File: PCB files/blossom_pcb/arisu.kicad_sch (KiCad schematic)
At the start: 40 parts, among them P1 Conn_ARM_JTAG_SWD_10

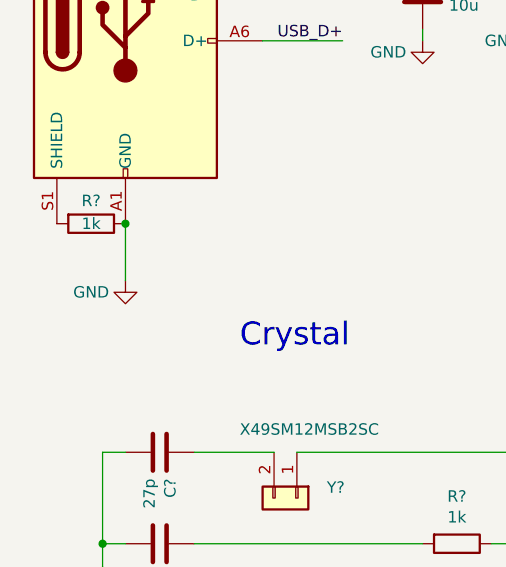
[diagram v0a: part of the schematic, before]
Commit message: Fixed part numbers for JLCPCB
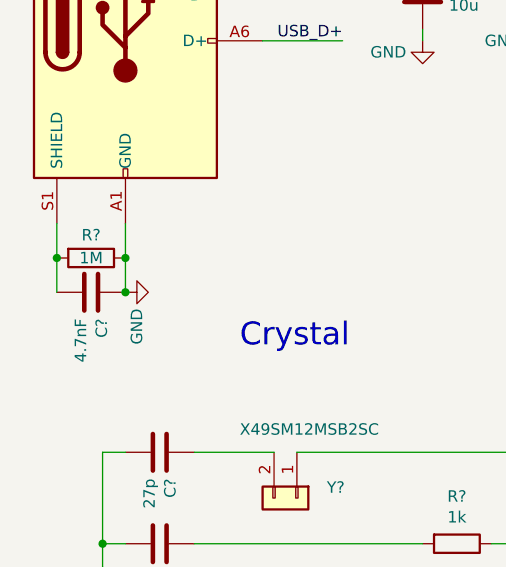
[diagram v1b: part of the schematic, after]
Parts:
- removed R?: 1k, Resistor_SMD:R_01005_0402Metric, symbol arisu-rescue:R-Device
- added C?: 4.7nF, Capacitor_SMD:C_0201_0603Metric, symbol arisu-rescue:C-Device
- added R?: 1M, Resistor_SMD:R_0805_2012Metric, symbol arisu-rescue:R-Device
- R? (x2): MPN (none) -> C104384
- USB1: MPN (none) -> C134092
- Y?: MPN (none) -> C110563
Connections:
- net GND: now also C?.1, R?.1
- net at USB1.S1 (SHIELD): now also C?.2, R?.2
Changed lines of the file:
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@@
   (junction (at 158.75 43.18) (diameter 0) (color 0 0 0 0)
   )
-  (junction (at 26.67 59.69) (diameter 0) (color 0 0 0 0)
-  )
   (junction (at 158.75 48.26) (diameter 0) (color 0 0 0 0)
   )
@@
   (junction (at 121.92 43.18) (diameter 0) (color 0 0 0 0)
   )
+  (junction (at 26.67 67.31) (diameter 0) (color 0 0 0 0)
+  )
   (junction (at 148.59 48.26) (diameter 0) (color 0 0 0 0)
   )
@@
   (junction (at 172.72 39.37) (diameter 0) (color 0 0 0 0)
   )
+  (junction (at 19.05 63.5) (diameter 0) (color 0 0 0 0)
+  )
   (junction (at 207.01 39.37) (diameter 0) (color 0 0 0 0)
   )
+  (junction (at 26.67 63.5) (diameter 0) (color 0 0 0 0)
+  )
   (junction (at 151.13 48.26) (diameter 0) (color 0 0 0 0)
   )
@@
     (stroke (width 0) (type default))
   )
-  (wire (pts (xy 26.67 66.04) (xy 26.67 59.69))
-    (stroke (width 0) (type default))
-  )
   (bus (pts (xy 220.98 97.79) (xy 220.98 100.33))
     (stroke (width 0) (type default))
@@
     (stroke (width 0) (type default))
   )
+  (wire (pts (xy 19.05 63.5) (xy 19.05 59.69))
+    (stroke (width 0) (type default))
+  )
   (bus (pts (xy 213.36 111.76) (xy 213.36 114.3))
     (stroke (width 0) (type default))
@@
     (stroke (width 0) (type default))
   )
+  (wire (pts (xy 26.67 63.5) (xy 26.67 67.31))
+    (stroke (width 0) (type default))
+  )
   (wire (pts (xy 138.43 27.94) (xy 149.86 27.94))
     (stroke (width 0) (type default))
@@
     (stroke (width 0) (type default))
   )
+  (wire (pts (xy 19.05 63.5) (xy 19.05 67.31))
+    (stroke (width 0) (type default))
+  )
+  (wire (pts (xy 26.67 63.5) (xy 26.67 59.69))
+    (stroke (width 0) (type default))
+  )
   (wire (pts (xy 173.99 114.3) (xy 210.82 114.3))
     (stroke (width 0) (type default))
@@
       (effects (font (size 1.27 1.27)) hide)
     )
+    (property "MPN" "C110563" (at 45.72 90.17 0)
+      (effects (font (size 1.27 1.27)) hide)
+    )
     (pin "1")
     (pin "2")
@@
     )
   )
+  (symbol (lib_id "arisu-rescue:R-Device") (at 22.86 63.5 270) (unit 1)
+    (in_bom yes) (on_board yes) (dnp no)
+    (property "Reference" "R?" (at 22.86 60.96 90)
+      (effects (font (size 1.27 1.27)))
+    )
+    (property "Value" "1M" (at 22.86 63.5 90)
+      (effects (font (size 1.27 1.27)))
+    )
+    (property "Footprint" "Resistor_SMD:R_0805_2012Metric" (at 22.86 61.722 90)
+      (effects (font (size 1.27 1.27)) hide)
+    )
+    (property "Datasheet" "~" (at 22.86 63.5 0)
+      (effects (font (size 1.27 1.27)) hide)
+    )
+    (property "MPN" "C17514" (at 22.86 63.5 0)
+      (effects (font (size 1.27 1.27)) hide)
+    )
+    (pin "1")
+    (pin "2")
+    (instances
+      (project "RP2040_minimal"
+        (path "/4e80874f-13b9-4886-a592-f501191b7905"
+          (reference "R?") (unit 1)
+        )
+      )
+      (project "arisu"
+        (path "/6a4507f9-fb93-401b-b9e1-9f2bcbbd5186"
+          (reference "R9") (unit 1)
+        )
+      )
+    )
+  )
   (symbol (lib_id "PCM_RP2040_minimal-rescue:VBUS-power") (at 29.21 114.3 0) (unit 1)
     (in_bom yes) (on_board yes) (dnp no)
@@
     )
   )
+  (symbol (lib_id "arisu-rescue:C-Device") (at 22.86 67.31 270) (unit 1)
+    (in_bom yes) (on_board yes) (dnp no)
+    (property "Reference" "C?" (at 24.0284 70.231 0)
+      (effects (font (size 1.27 1.27)) (justify left))
+    )
+    (property "Value" "4.7nF" (at 21.717 70.231 0)
+      (effects (font (size 1.27 1.27)) (justify left))
+    )
+    (property "Footprint" "Capacitor_SMD:C_0201_0603Metric" (at 19.05 68.2752 0)
+      (effects (font (size 1.27 1.27)) hide)
+    )
+    (property "Datasheet" "~" (at 22.86 67.31 0)
+      (effects (font (size 1.27 1.27)) hide)
+    )
+    (pin "1")
+    (pin "2")
+    (instances
+      (project "RP2040_minimal"
+        (path "/4e80874f-13b9-4886-a592-f501191b7905"
+          (reference "C?") (unit 1)
+        )
+      )
+      (project "arisu"
+        (path "/6a4507f9-fb93-401b-b9e1-9f2bcbbd5186"
+          (reference "C18") (unit 1)
+        )
+      )
+    )
+  )
   (symbol (lib_id "arisu-rescue:R-Device") (at 45.72 25.4 270) (unit 1)
     (in_bom yes) (on_board yes) (dnp no)
@@
       (effects (font (size 1.27 1.27)) hide)
     )
+    (property "MPN" "C104384" (at 45.72 25.4 0)
+      (effects (font (size 1.27 1.27)) hide)
+    )
     (pin "1")
     (pin "2")
@@
       (effects (font (size 1.27 1.27)) hide)
     )
+    (property "MPN" "C134092" (at 26.67 36.83 0)
+      (effects (font (size 1.27 1.27)) hide)
+    )
     (pin "A1")
     (pin "A12")
@@
     )
   )
-  (symbol (lib_id "arisu-rescue:GND-power") (at 26.67 66.04 0) (unit 1)
+  (symbol (lib_id "arisu-rescue:GND-power") (at 26.67 67.31 90) (unit 1)
     (in_bom yes) (on_board yes) (dnp no)
-    (property "Reference" "#PWR?" (at 26.67 72.39 0)
+    (property "Reference" "#PWR?" (at 33.02 67.31 0)
       (effects (font (size 1.27 1.27)) hide)
     )
-    (property "Value" "GND" (at 22.86 67.31 0)
+    (property "Value" "GND" (at 27.94 71.12 0)
       (effects (font (size 1.27 1.27)))
     )
-    (property "Footprint" "" (at 26.67 66.04 0)
+    (property "Footprint" "" (at 26.67 67.31 0)
       (effects (font (size 1.27 1.27)) hide)
     )
-    (property "Datasheet" "" (at 26.67 66.04 0)
+    (property "Datasheet" "" (at 26.67 67.31 0)
       (effects (font (size 1.27 1.27)) hide)
     )
@@
     )
   )
-  (symbol (lib_id "arisu-rescue:R-Device") (at 22.86 59.69 270) (unit 1)
-    (in_bom yes) (on_board yes) (dnp no)
-    (property "Reference" "R?" (at 22.86 57.15 90)
-      (effects (font (size 1.27 1.27)))
-    )
-    (property "Value" "1k" (at 22.86 59.69 90)
-      (effects (font (size 1.27 1.27)))
-    )
-    (property "Footprint" "Resistor_SMD:R_01005_0402Metric" (at 22.86 57.912 90)
-      (effects (font (size 1.27 1.27)) hide)
-    )
-    (property "Datasheet" "~" (at 22.86 59.69 0)
-      (effects (font (size 1.27 1.27)) hide)
-    )
-    (pin "1")
-    (pin "2")
-    (instances
-      (project "RP2040_minimal"
-        (path "/4e80874f-13b9-4886-a592-f501191b7905"
-          (reference "R?") (unit 1)
-        )
-      )
-      (project "arisu"
-        (path "/6a4507f9-fb93-401b-b9e1-9f2bcbbd5186"
-          (reference "R8") (unit 1)
-        )
-      )
-    )
-  )
   (symbol (lib_id "arisu-rescue:MountingHole-Mechanical") (at 267.97 45.72 0) (unit 1)
     (in_bom yes) (on_board yes) (dnp no)
@@
       (effects (font (size 1.27 1.27)) hide)
     )
+    (property "MPN" "C104384" (at 45.72 30.48 0)
+      (effects (font (size 1.27 1.27)) hide)
+    )
